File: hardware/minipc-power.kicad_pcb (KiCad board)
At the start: 4 copper layers, 50 x 34 mm, 104 parts, among them J1 USB-C HRO TYPE-C-31-M-12, J10 VSYS (switch), J11 CHG, J12 PG_CHG, J13 VBAT_SENSE, J14 3V3_PG, J15 GND, J16 GND, J17 GND, J2 BAT+, J3 BAT-, J4 NTC, J5 NTC-, J6 +12V OUT, J7 +5V OUT, J8 +3V3 OUT, J9 EN (switch), Q1 CSD13202Q2, Q2 CSD13202Q2, Q3 CSD13202Q2, Q4 CSD25404Q3, Q5 CSD25404Q3, Q6 2N7002, U1 CH224Q, U2 BQ25606, U3 HY2113-MB1A, U4 TPS61178, U5 TPS61088-Q1, U6 TPS63802

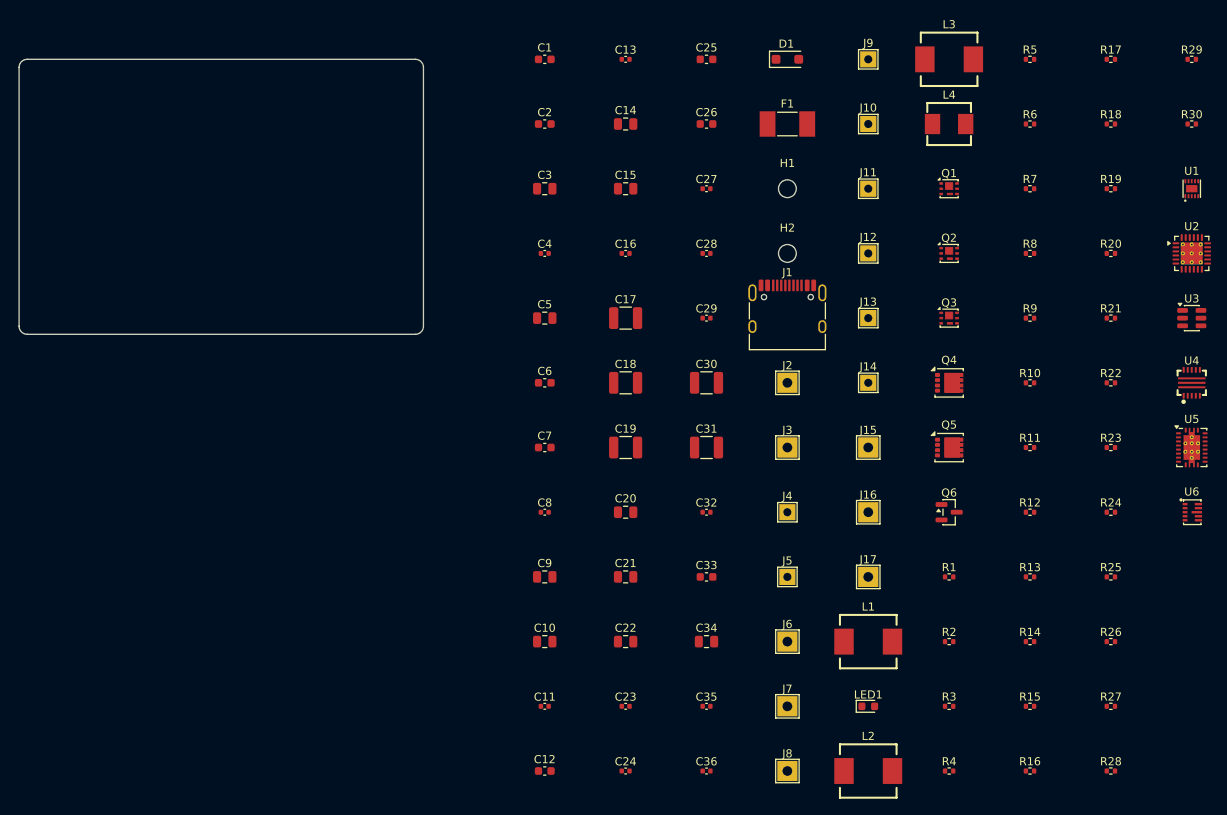
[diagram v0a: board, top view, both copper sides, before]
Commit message: Board placement v1: three bands, converters per datasheet layout examples, 0 courtyard overlaps
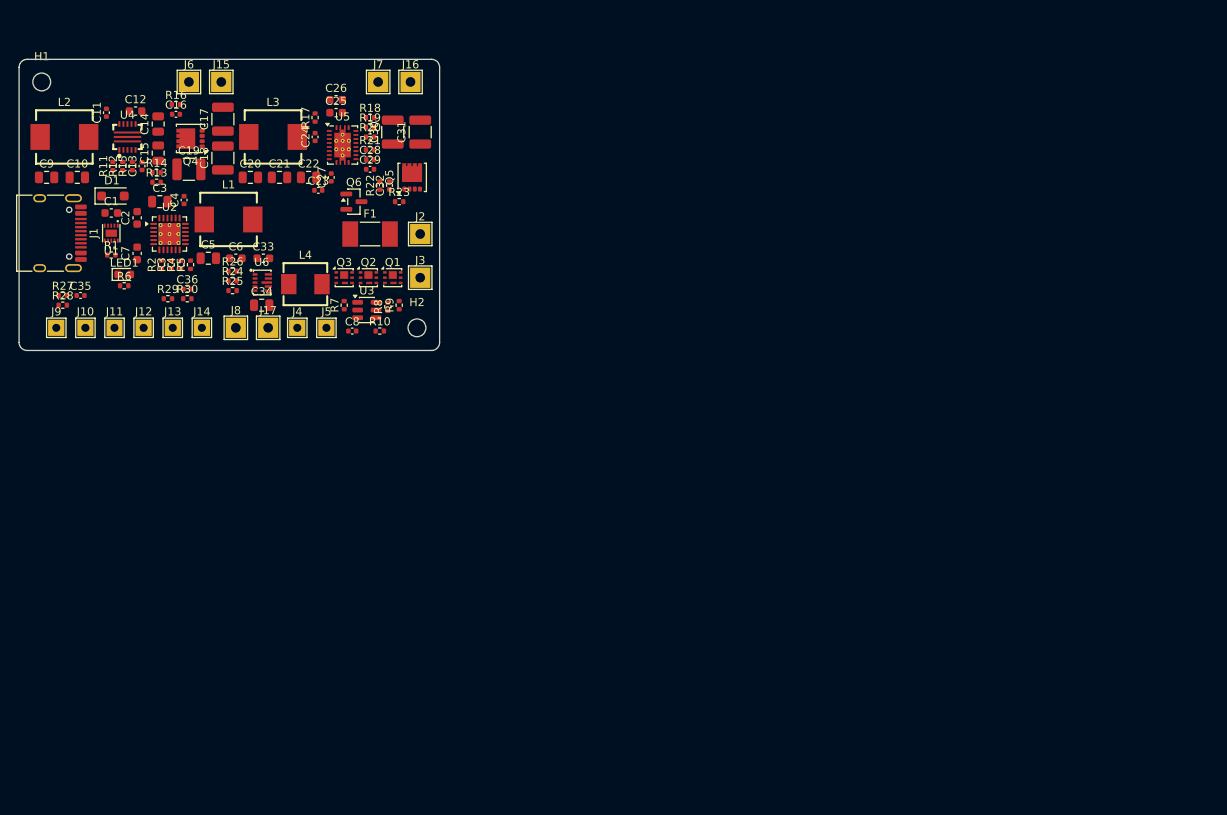
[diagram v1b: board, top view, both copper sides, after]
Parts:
- moved R28 141.8 mm to (105.4, 130.4)
- moved R27 139.2 mm to (105.4, 129.2)
- moved U4 135.1 mm to (113.4, 109.6)
- moved R16 133.9 mm to (119.4, 105.6)
- moved U1 133.7 mm to (111.4, 121.5), turned to 180 degrees
- moved R29 130.0 mm to (118.4, 129.6)
- moved R15 129.6 mm to (114.0, 113.2), turned to 90 degrees
- moved L2 126.6 mm to (105.6, 109.6)
- moved U2 126.4 mm to (118.6, 121.6)
- moved R30 126.1 mm to (120.8, 129.6)
- moved R14 122.6 mm to (117.0, 114.0)
- moved R12 120.1 mm to (112.8, 113.2), turned to 90 degrees
- moved R11 118.6 mm to (111.6, 113.2), turned to 90 degrees
- moved R13 118.5 mm to (117.0, 115.2)
- moved U6 118.5 mm to (130.0, 127.6)
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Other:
- board size 50 x 34 mm -> 52 x 36 mm

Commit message: Pad labels on both silkscreens, round GND/negative pads, refs moved to fab layer, 3D models for F1 and J1
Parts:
- J15, J16, J17, J3: footprint TestPoint:TestPoint_THTPad_2.5x2.5mm_Drill1.2mm -> TestPoint:TestPoint_THTPad_D2.5mm_Drill1.2mm
- J5: footprint TestPoint:TestPoint_THTPad_2.0x2.0mm_Drill1.0mm -> TestPoint:TestPoint_THTPad_D2.0mm_Drill1.0mm
- moved C16 3.50 mm to (117.6, 103.8)
- moved R16 1.90 mm to (117.6, 105.0)
- moved C17 1.00 mm to (125.2, 108.4)
- moved C18 1.00 mm to (125.2, 113.2)
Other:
- board text added: "+12V"
- board text added: "+3V3"
- board text added: "+5V"
- board text added: "BAT+"
- board text added: "BAT-"
- board text added: "CHG"
- board text added: "GND"
- board text added: "NTC"
- board text added: "PG"
- board text added: "PG3"
- board text added: "SW"
- board text added: "VBAT"

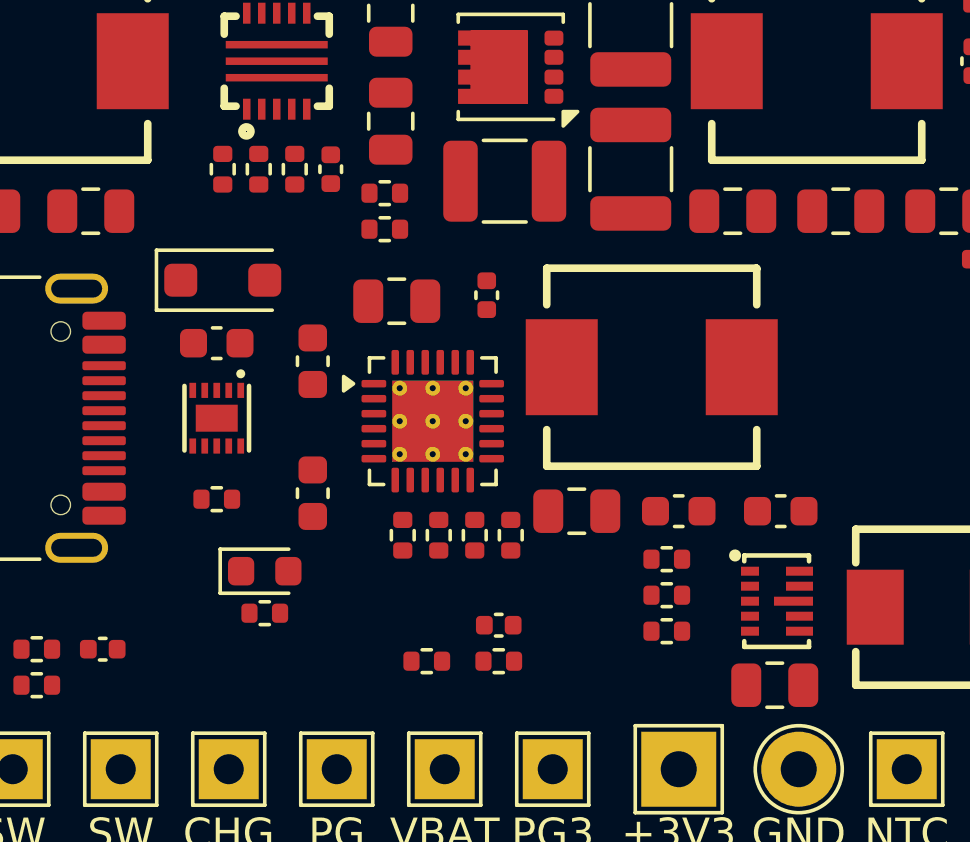
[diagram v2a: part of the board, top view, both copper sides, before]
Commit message: Drop CH224Q D+/D- (PD uses CC), re-orient U1, charger-area placement for routability; routing infrastructure
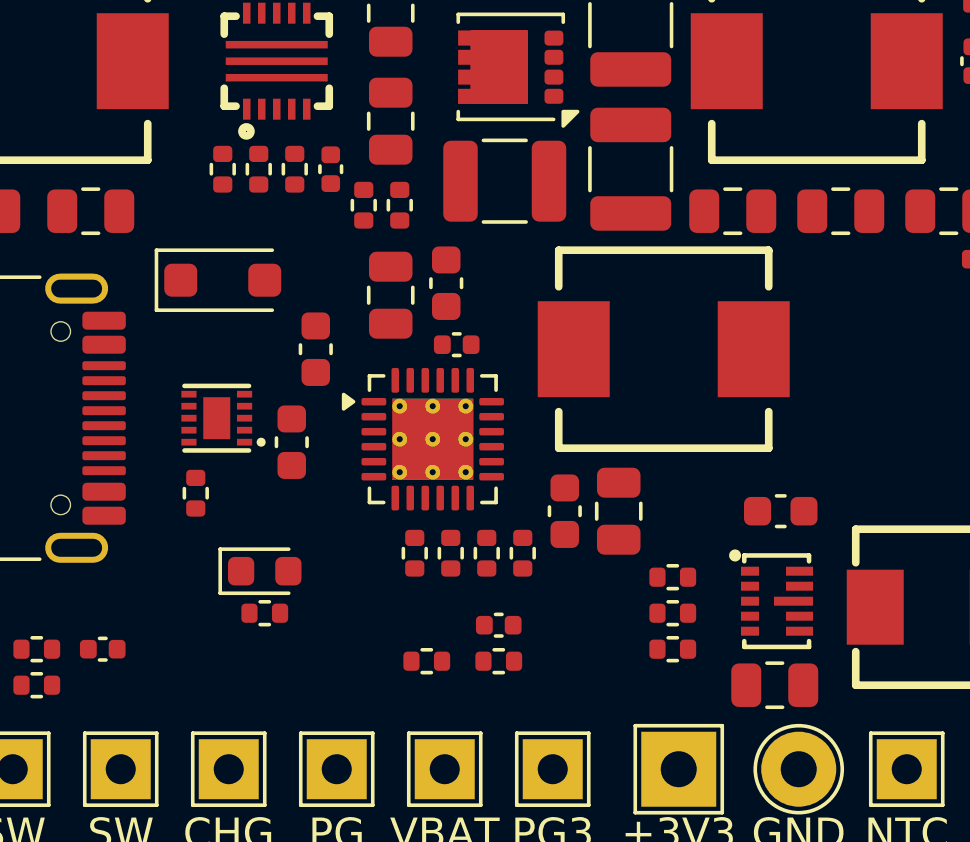
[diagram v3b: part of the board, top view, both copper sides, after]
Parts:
- moved C7 8.29 mm to (119.0, 117.0)
- moved C1 4.14 mm to (113.9, 122.3), turned to 90 degrees
- moved C6 3.80 mm to (123.0, 124.6), turned to 90 degrees
- moved C4 1.93 mm to (119.4, 119.0), turned to 0 degrees
- moved C5 1.40 mm to (124.8, 124.6), turned to 90 degrees
- moved R13 1.06 mm to (116.3, 114.4), turned to 90 degrees
- moved R1 0.73 mm to (110.7, 124.0), turned to 90 degrees
- moved R2 0.72 mm to (118.0, 126.0), turned to -90 degrees
- moved R3 0.72 mm to (119.2, 126.0), turned to -90 degrees
- moved R4 0.72 mm to (120.4, 126.0)
- moved L1 0.72 mm to (126.3, 119.2)
- moved R5 0.72 mm to (121.6, 126.0), turned to -90 degrees
- moved R14 0.64 mm to (117.5, 114.4), turned to 90 degrees
- moved R24 0.63 mm to (126.6, 128.0)
- moved R26 0.63 mm to (126.6, 126.8)
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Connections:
- J1 pad A6: Net-(U1-DP) -> unconnected-(J1-D+-PadA6)
- J1 pad A7: Net-(U1-DM) -> unconnected-(J1-D--PadA7)
- J1 pad B6: Net-(U1-DP) -> unconnected-(J1-D+-PadB6)
- J1 pad B7: Net-(U1-DM) -> unconnected-(J1-D--PadB7)
- U1 pad 4: Net-(U1-DP) -> unconnected-(U1-DP-Pad4)
- U1 pad 5: Net-(U1-DM) -> unconnected-(U1-DM-Pad5)

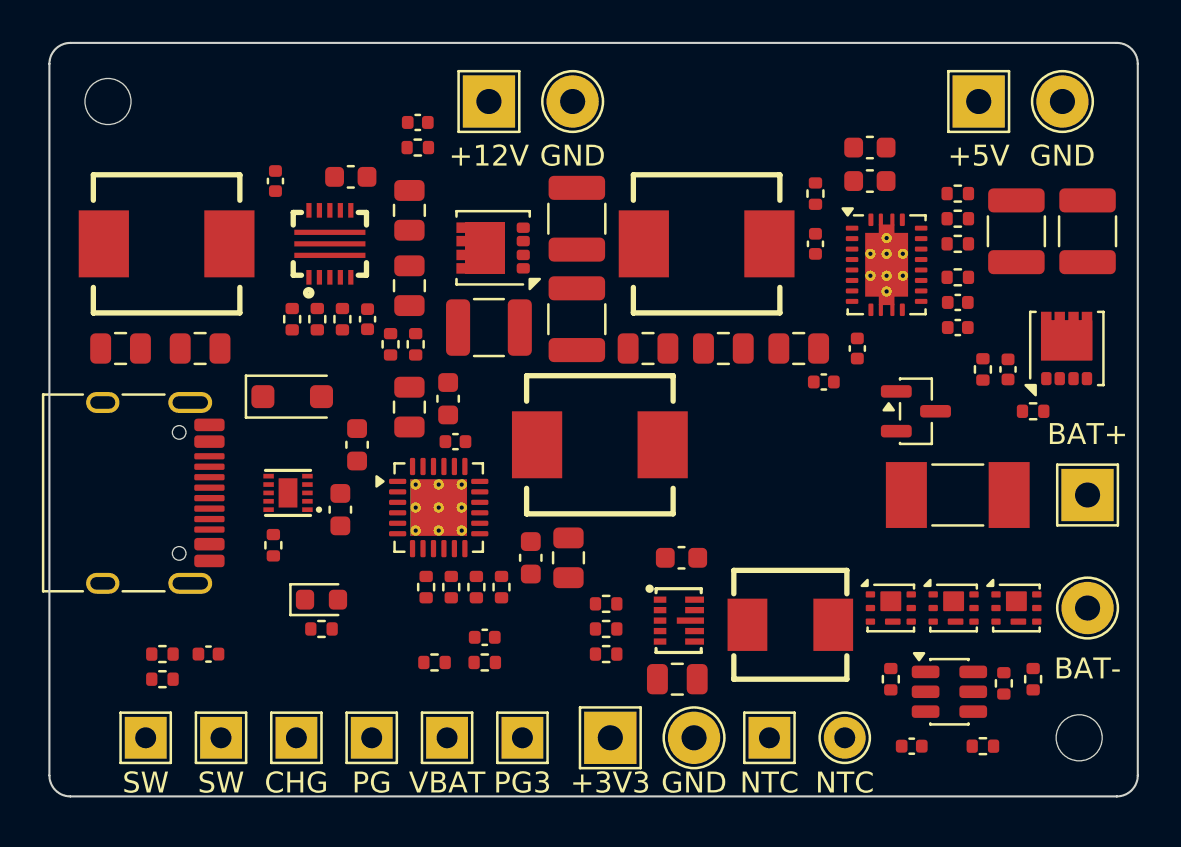
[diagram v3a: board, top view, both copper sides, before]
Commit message: Route USB/PD, charger and protection; FETs alternate orientation; router keeps via holes apart
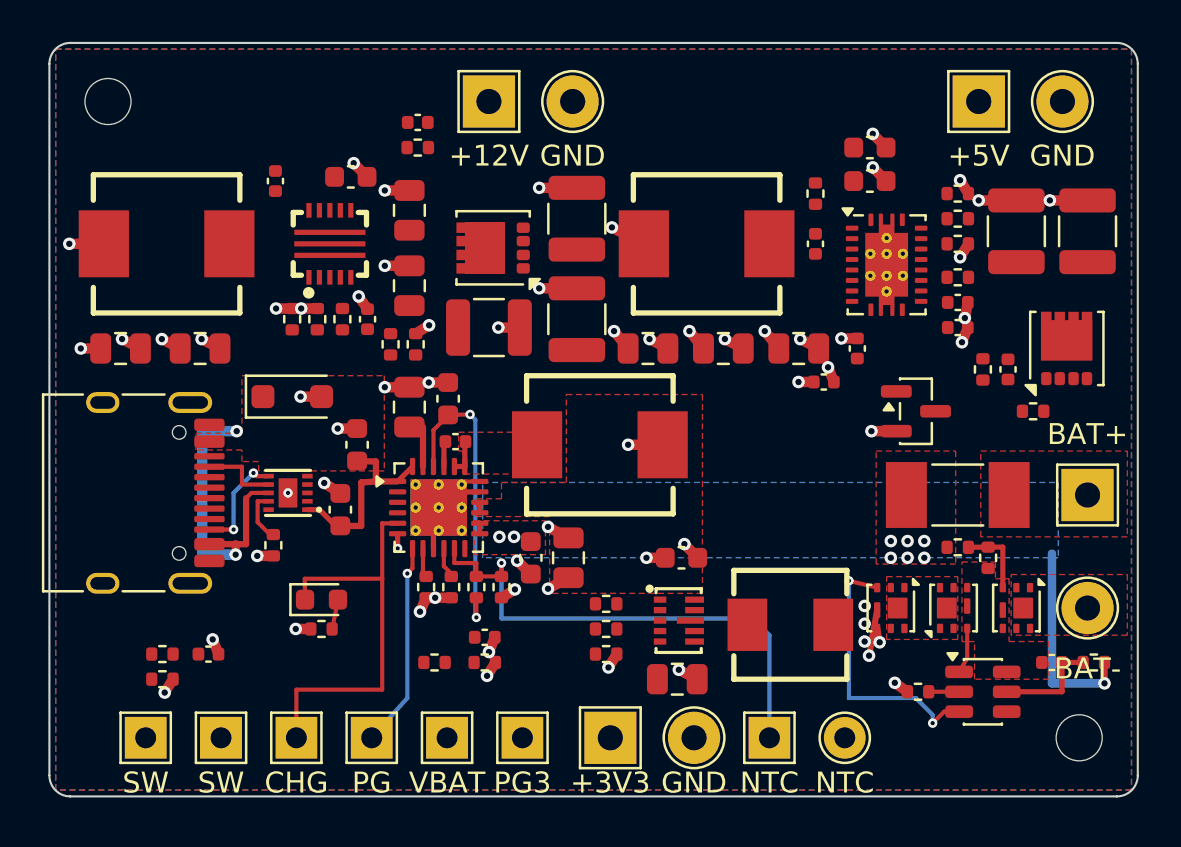
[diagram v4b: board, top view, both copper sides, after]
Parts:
- moved R7 9.73 mm to (149.9, 129.6), turned to 180 degrees
- moved R10 9.00 mm to (144.8, 124.6), turned to -90 degrees
- moved C8 7.80 mm to (147.9, 129.6), turned to 180 degrees
- moved R9 7.26 mm to (143.4, 124.1), turned to 0 degrees
- moved R8 4.12 mm to (141.5, 131.0), turned to 180 degrees
- moved U3 1.60 mm to (144.6, 131.0)
- turned C6 to -90 degrees
- turned F1 to 180 degrees
- turned Q1 to -90 degrees
- turned Q2 to 90 degrees
- turned Q3 to -90 degrees
- turned R1 to -90 degrees
- turned R6 to 180 degrees
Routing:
- net GND: track 0.00 -> 50.0 mm, vias 0 -> 52
- net Net-(U2-TS): track 0.00 -> 24.9 mm, vias 0 -> 1
- net VBUS: track 0.00 -> 24.3 mm, vias 0 -> 2
- net Net-(LED1-K): track 0.00 -> 19.8 mm
- net Net-(U2-REGN): track 0.00 -> 14.6 mm, vias 0 -> 2
- net VSYS: track 0.00 -> 14.1 mm, vias 0 -> 12
- net Net-(Q3-G): track 0.00 -> 13.2 mm, vias 0 -> 2
- net BAT: track 0.00 -> 10.2 mm, vias 0 -> 9
- net /PG_CHG: track 0.00 -> 9.79 mm, vias 0 -> 1
- net Net-(U3-VDD): track 0.00 -> 5.05 mm
- net Net-(J1-CC2): track 0.00 -> 5.03 mm, vias 0 -> 2
- net Net-(J1-CC1): track 0.00 -> 3.68 mm
- net Net-(Q1-G): track 0.00 -> 3.58 mm
- net Net-(U1-CFG1): track 0.00 -> 2.52 mm
- net Net-(Q2-G): track 0.00 -> 2.18 mm
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- added copper zone on B.Cu, net BAT
- added copper zone on F.Cu, net BAT
- added copper zone on B.Cu, net GND
- added copper zone on F.Cu, net GND
- added copper zone on In1.Cu, net GND
- added copper zone on F.Cu, net Net-(C4-Pad2)
- added copper zone on F.Cu, net Net-(F1-Pad1)
- added copper zone on F.Cu, net Net-(J3-Pad1)
- added copper zone on F.Cu, net Net-(Q2-D-Pad1)
- added copper zone on F.Cu, net Net-(U3-VSS)
- added copper zone on F.Cu, net VBUS
- added copper zone on F.Cu, net VSYS
- added copper zone on In2.Cu, net VSYS

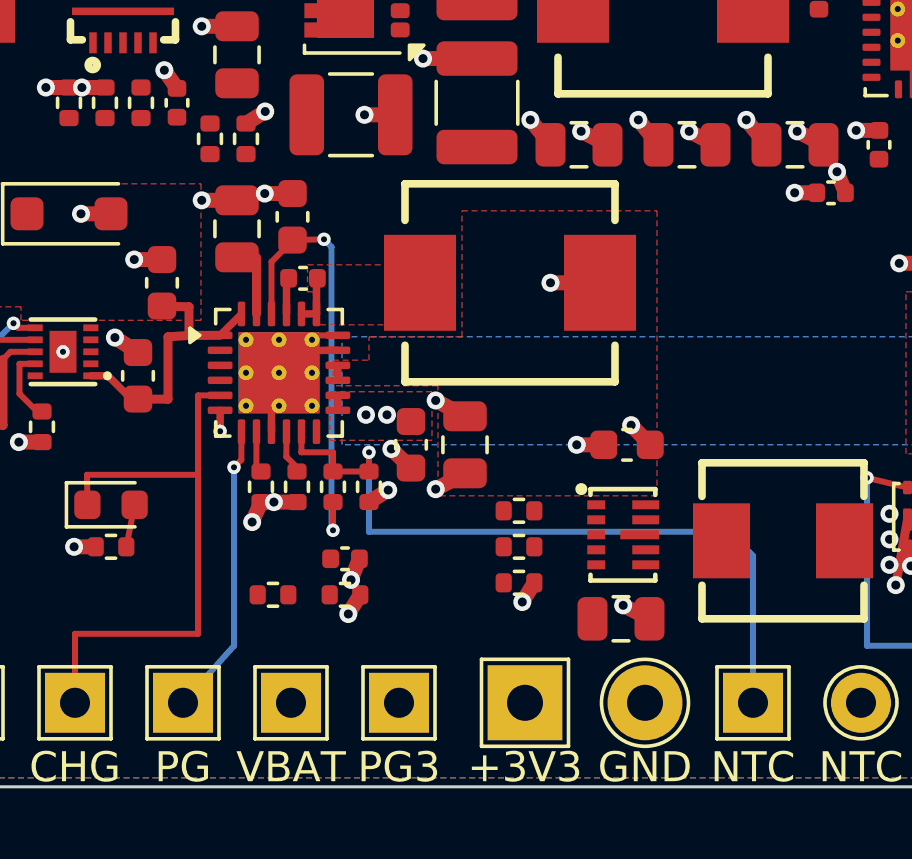
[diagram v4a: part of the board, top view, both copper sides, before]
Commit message: Charger to datasheet fig. 12-2: C_SYS at SYS/GND pins, single-point analog ground with pour keepout; compliance log; gap 21
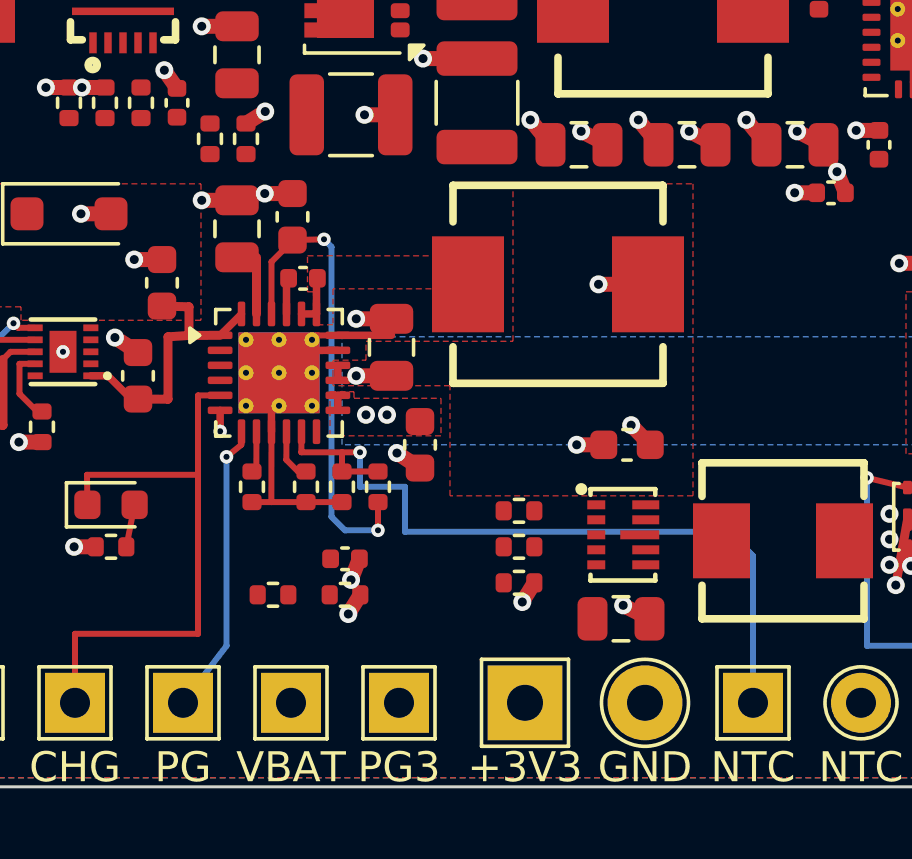
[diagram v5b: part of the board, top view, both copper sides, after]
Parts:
- moved C5 4.07 mm to (122.3, 121.3)
- moved L1 1.60 mm to (127.9, 119.2)
- moved R4 1.50 mm to (121.9, 126.0)
- moved R5 0.90 mm to (120.7, 126.0)
- moved C6 0.30 mm to (123.3, 124.6)
- moved R2 0.30 mm to (117.7, 126.0)
- moved R3 0.30 mm to (119.5, 126.0)
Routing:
- net GND: track 50.0 -> 55.0 mm, vias 52 -> 49
- net Net-(U2-REGN): track 14.6 -> 15.8 mm
- net Net-(U2-TS): track 24.9 -> 25.5 mm
